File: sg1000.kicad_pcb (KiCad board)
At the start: 2 copper layers, 4 parts, among them U1 CY62256N, U2 PLCCZ80

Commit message: Just more TODO
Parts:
- added SW1: Pause Key, Button_Switch_THT:SW_PUSH_6mm, F.Cu at (129.4, 108.1)
- added U3: SN76489AN, Package_DIP:DIP-16_W7.62mm_LongPads, F.Cu at (117.8, 108.2)
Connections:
- net Net-(U1-Pad20) renamed /~CS_WRAM
- net Net-(U2-Pad18) renamed /~INT
- net Net-(U2-Pad19) renamed /~NMI
- net Net-(U2-Pad20) renamed /~HALT
- net Net-(U2-Pad21) renamed /~MERQ
- net Net-(U2-Pad22) renamed /~IORQ
- net Net-(U2-Pad30) renamed /~RESET
- net Net-(U2-Pad31) renamed /~M1
- net Net-(U2-Pad32) renamed /~RFSH
- U1 pad 22: Net-(U1-Pad22) -> /~RD
- U1 pad 27: Net-(U1-Pad27) -> /~WR
- U2 pad 23: Net-(U2-Pad23) -> /~RD
- U2 pad 26: Net-(U2-Pad26) -> /~WR
- U2 pad 28: Net-(U2-Pad28) -> /~WAIT
- U2 pad 29: Net-(U2-Pad29) -> +5V
- U2 pad 7: Net-(U2-Pad7) -> /CLK

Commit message: Decoders
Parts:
- added U13: 74LS139, Package_DIP:DIP-16_W7.62mm_LongPads, F.Cu at (93.9, 105.6)
- added U16: 74LS32, Package_DIP:DIP-14_W7.62mm_LongPads, F.Cu at (105.5, 105.6)
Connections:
- U2 pad 21: /~MERQ -> /~MREQ

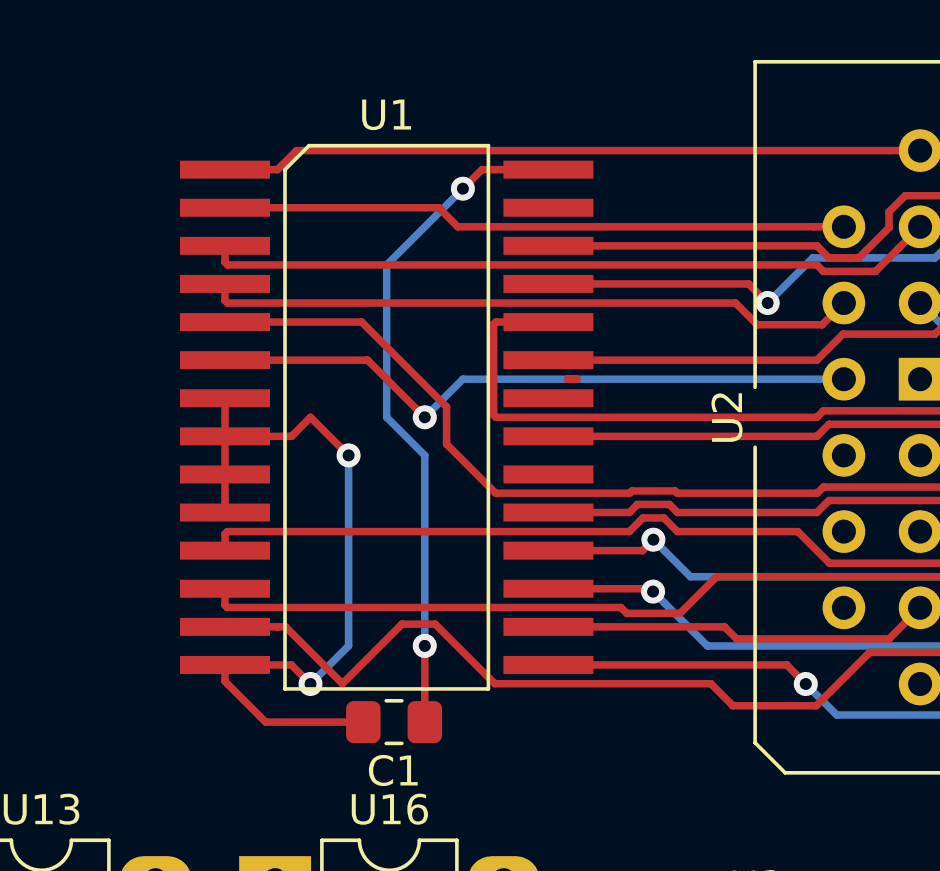
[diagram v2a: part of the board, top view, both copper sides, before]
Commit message: Use DIP 62256
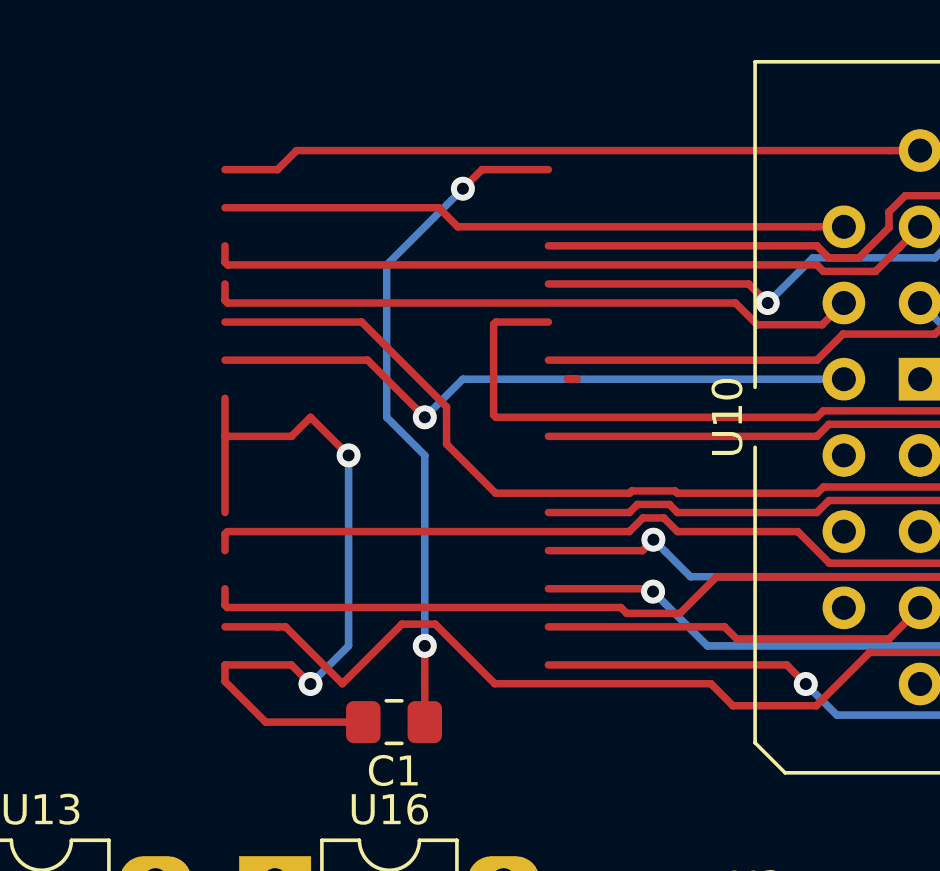
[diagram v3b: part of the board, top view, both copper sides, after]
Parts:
- removed U1: CY62256N, LeadedSolder:CY62256N
- renumbered U2 to U10

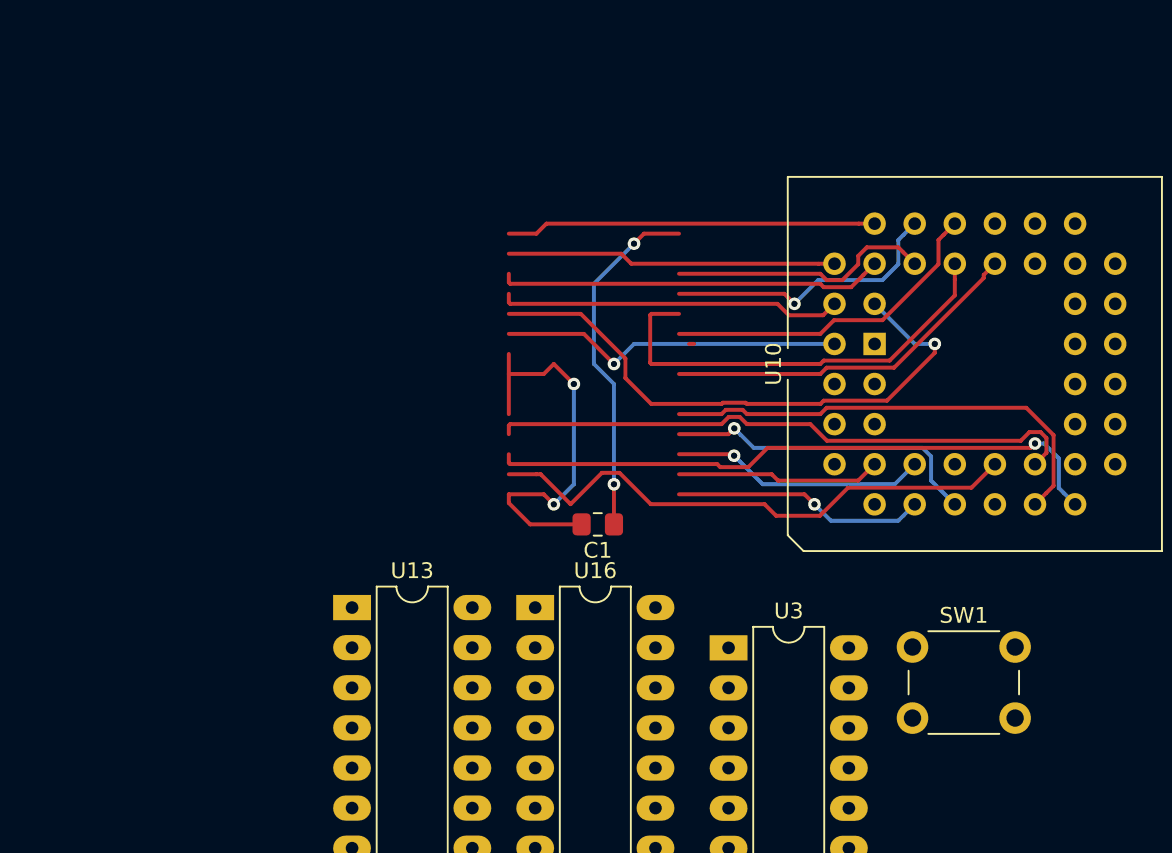
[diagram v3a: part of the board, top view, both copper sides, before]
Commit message: 0805 for resistors
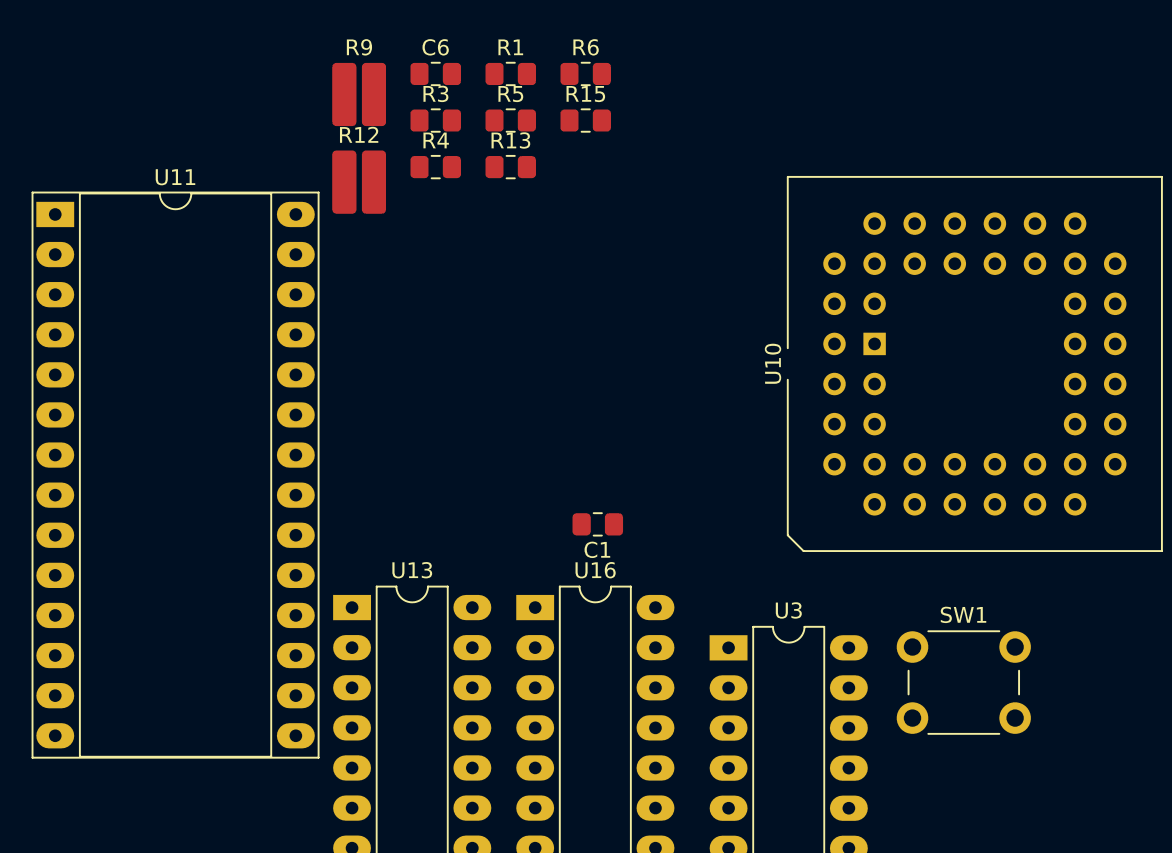
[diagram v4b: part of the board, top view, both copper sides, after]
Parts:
- added C6: 10µF, Capacitor_SMD:C_0805_2012Metric_Pad1.15x1.40mm_HandSolder, F.Cu at (99.2, 71.8)
- added R1: 100Ω, Resistor_SMD:R_0805_2012Metric_Pad1.15x1.40mm_HandSolder, F.Cu at (104.0, 71.8)
- added R12: 1kΩ, Resistor_SMD:R_0815_2038Metric_Pad1.53x4.00mm_HandSolder, F.Cu at (94.3, 78.7)
- added R13: 330Ω, Resistor_SMD:R_0805_2012Metric_Pad1.15x1.40mm_HandSolder, F.Cu at (104.0, 77.7)
- added R15: 330Ω, Resistor_SMD:R_0805_2012Metric_Pad1.15x1.40mm_HandSolder, F.Cu at (108.7, 74.8)
- added R3: 47kΩ, Resistor_SMD:R_0805_2012Metric_Pad1.15x1.40mm_HandSolder, F.Cu at (99.2, 74.8)
- added R4: 1kΩ, Resistor_SMD:R_0805_2012Metric_Pad1.15x1.40mm_HandSolder, F.Cu at (99.2, 77.7)
- added R5: 47kΩ, Resistor_SMD:R_0805_2012Metric_Pad1.15x1.40mm_HandSolder, F.Cu at (104.0, 74.8)
- added R6: 100Ω, Resistor_SMD:R_0805_2012Metric_Pad1.15x1.40mm_HandSolder, F.Cu at (108.7, 71.8)
- added R9: 540Ω, Resistor_SMD:R_0815_2038Metric_Pad1.53x4.00mm_HandSolder, F.Cu at (94.3, 73.1)
- added U11: AS6C62256-DIP, Package_DIP:DIP-28_W15.24mm_Socket_LongPads, F.Cu at (75.1, 80.7)
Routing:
- net /D1: track 39.8 -> 0.00 mm, vias 1 -> 0
- net /D0: track 37.8 -> 0.00 mm
- net /A9: track 36.9 -> 0.00 mm, vias 1 -> 0
- net /D2: track 34.9 -> 0.00 mm
- net /D7: track 29.7 -> 0.00 mm
- net /A2: track 28.0 -> 0.00 mm
- net GND: track 25.7 -> 0.00 mm, vias 2 -> 0
- net /A7: track 24.5 -> 0.00 mm
- net /A5: track 23.4 -> 0.00 mm
- net /A0: track 23.0 -> 0.00 mm
- net +5V: track 22.5 -> 0.00 mm, vias 2 -> 0
- net /A10: track 21.9 -> 0.00 mm, vias 1 -> 0
- net /A8: track 21.8 -> 0.00 mm
- net /A1: track 21.3 -> 0.00 mm
- net /A6: track 20.9 -> 0.00 mm
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
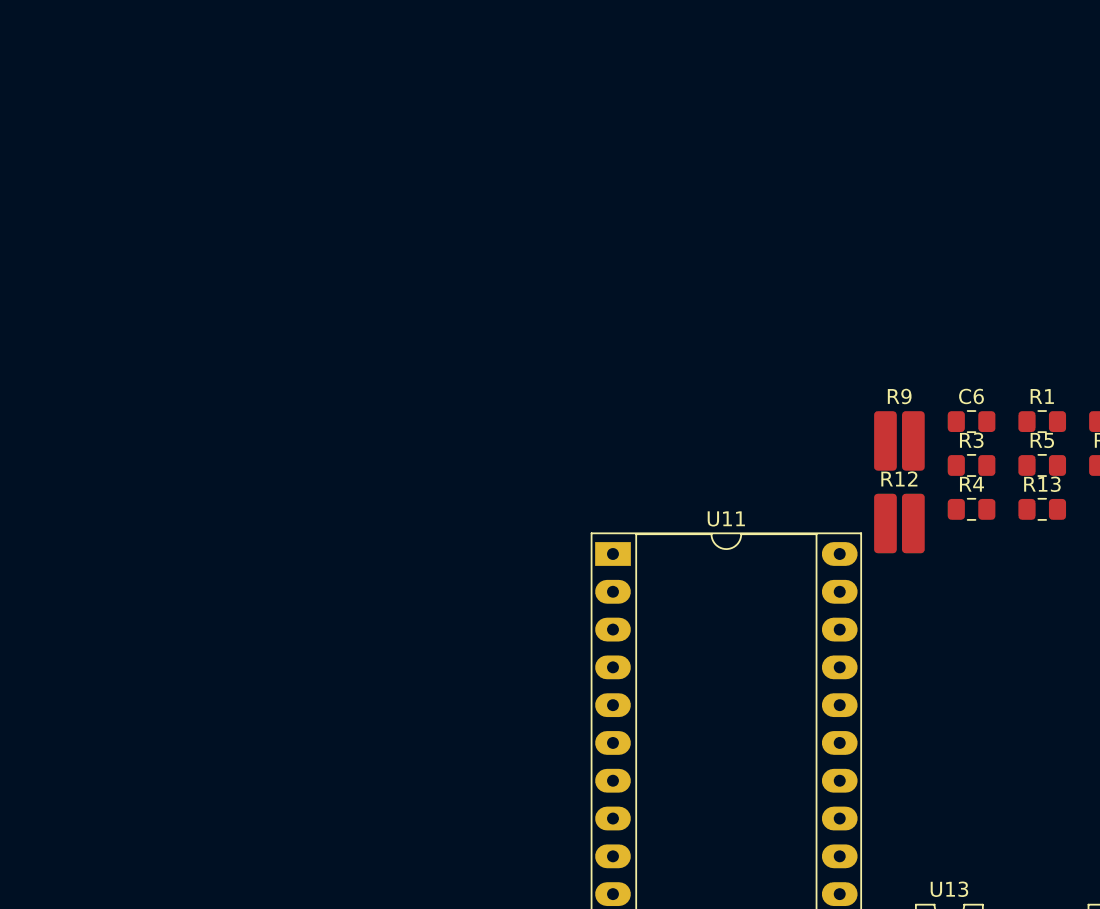
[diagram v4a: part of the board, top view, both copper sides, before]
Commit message: More footprints assigned
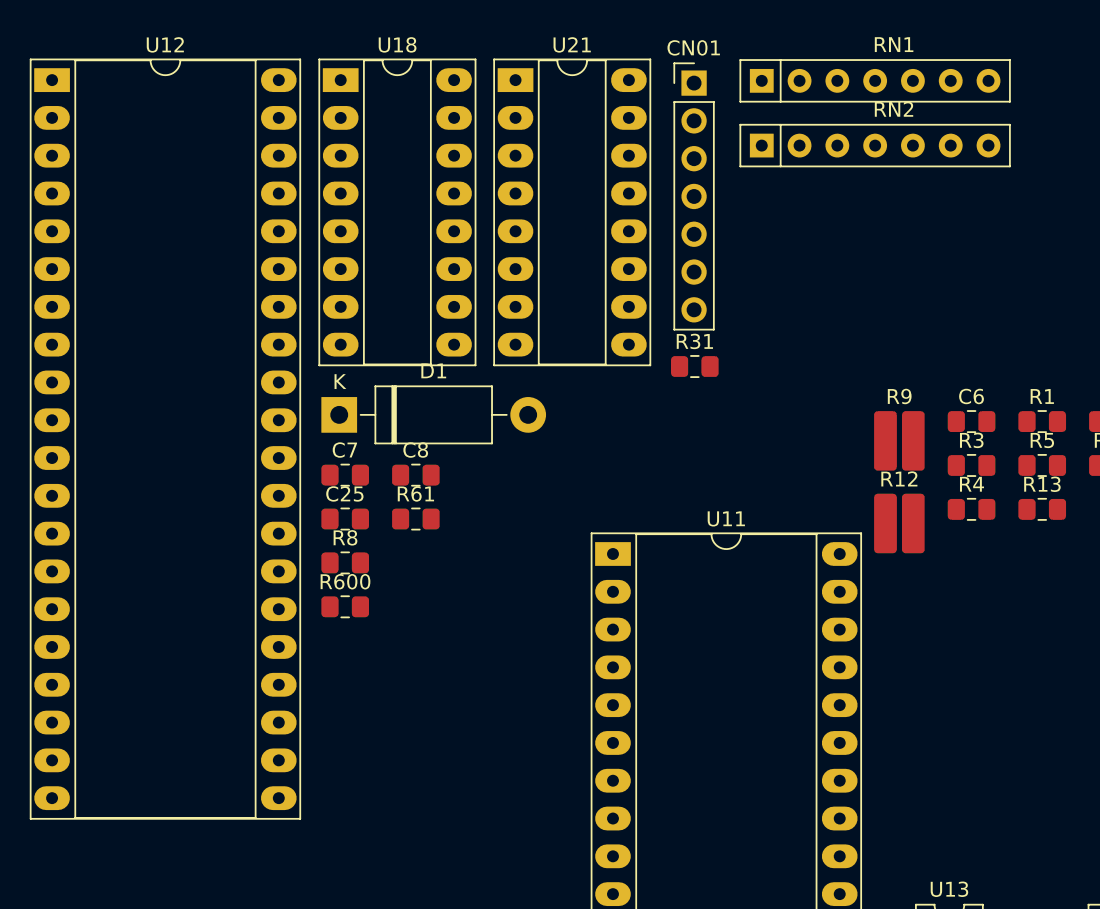
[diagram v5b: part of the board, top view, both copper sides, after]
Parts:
- added C25: 10µF, Capacitor_SMD:C_0805_2012Metric_Pad1.15x1.40mm_HandSolder, F.Cu at (57.1, 78.3)
- added C7: 33pF, Capacitor_SMD:C_0805_2012Metric_Pad1.15x1.40mm_HandSolder, F.Cu at (57.1, 75.4)
- added C8: 33pF, Capacitor_SMD:C_0805_2012Metric_Pad1.15x1.40mm_HandSolder, F.Cu at (61.9, 75.4)
- added CN01: Conn_01x07_Female, Connector_PinHeader_2.54mm:PinHeader_1x07_P2.54mm_Vertical, F.Cu at (80.5, 49.0)
- added D1: D, Diode_THT:D_DO-15_P12.70mm_Horizontal, F.Cu at (56.7, 71.3)
- added R31: 2.2kΩ, Resistor_SMD:R_0805_2012Metric_Pad1.15x1.40mm_HandSolder, F.Cu at (80.6, 68.1)
- added R600: 330Ω, Resistor_SMD:R_0805_2012Metric_Pad1.15x1.40mm_HandSolder, F.Cu at (57.1, 84.2)
- added R61: 560Ω, Resistor_SMD:R_0805_2012Metric_Pad1.15x1.40mm_HandSolder, F.Cu at (61.9, 78.3)
- added R8: 1MΩ, Resistor_SMD:R_0805_2012Metric_Pad1.15x1.40mm_HandSolder, F.Cu at (57.1, 81.3)
- added RN1: 4.7kΩ, Resistor_THT:R_Array_SIP7, F.Cu at (85.1, 48.9)
- added RN2: 4.7kΩ, Resistor_THT:R_Array_SIP7, F.Cu at (85.1, 53.2)
- added U12: TMS9918A, Package_DIP:DIP-40_W15.24mm_Socket_LongPads, F.Cu at (37.4, 48.9)
- added U18: 74LS257, Package_DIP:DIP-16_W7.62mm_Socket_LongPads, F.Cu at (56.8, 48.9)
- added U21: 74LS257, Package_DIP:DIP-16_W7.62mm_Socket_LongPads, F.Cu at (68.5, 48.9)
